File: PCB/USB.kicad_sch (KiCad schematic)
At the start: 30 parts, among them J1 DX07S024JJ2R1300, Q6 AGM612AP, U3 TPD4S480RUKR

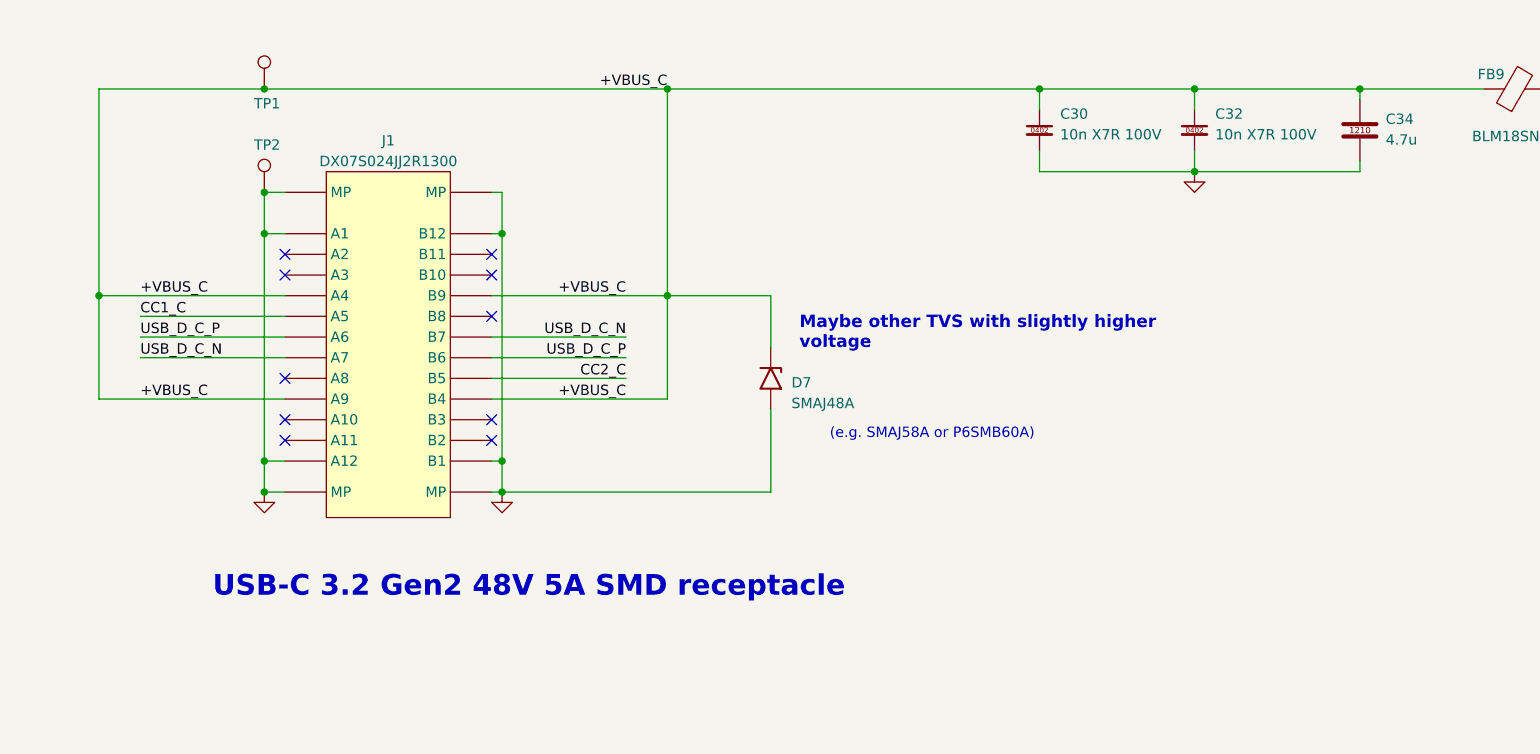
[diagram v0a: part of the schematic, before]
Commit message: Changed inductor to much better one
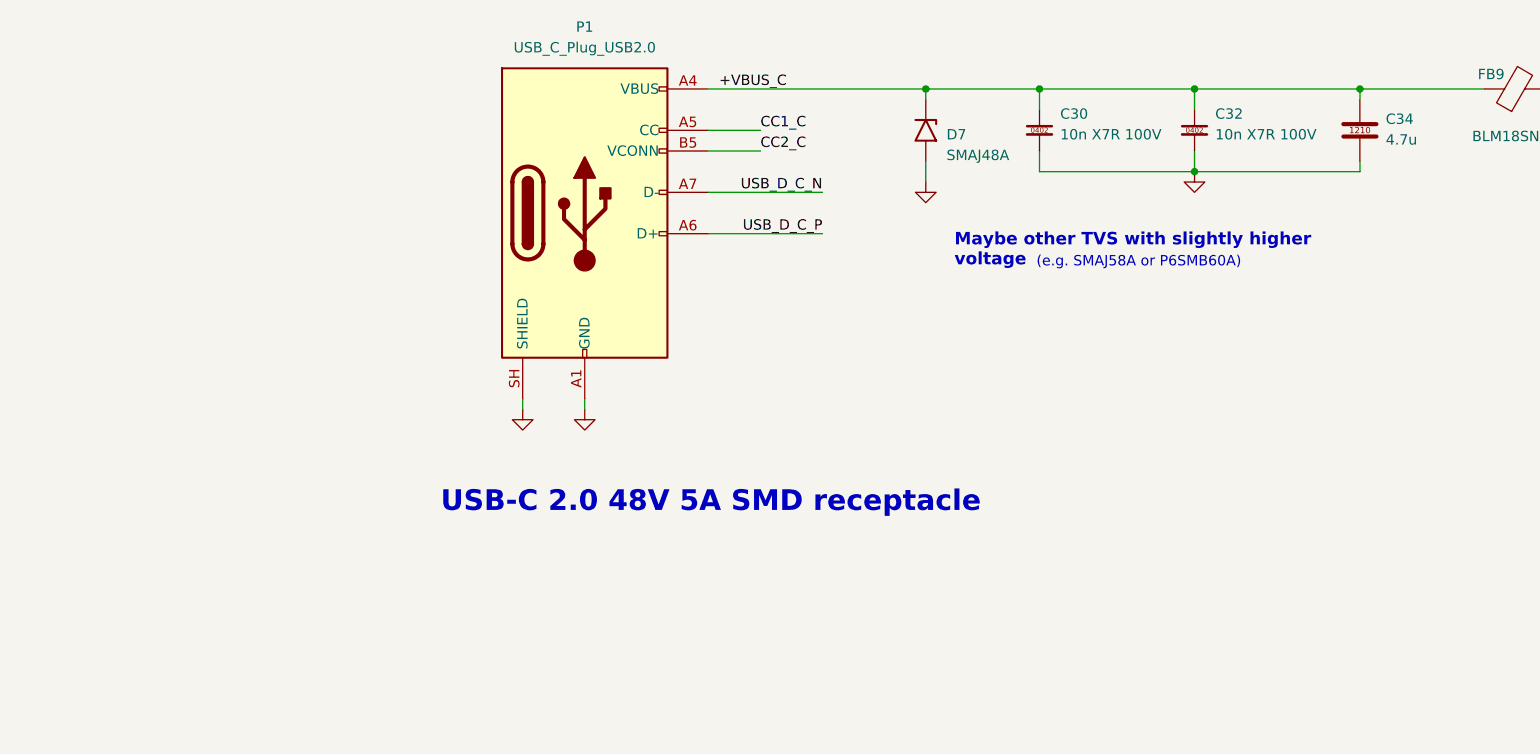
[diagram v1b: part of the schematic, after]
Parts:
- removed J1: DX07S024JJ2R1300, Altium_port:DX07S024JJ2R1300, symbol 0_PD240W:DX07S024JJ2R1300
- removed TP1, TP2: sp_oval_300x100, TestPoint:TestPoint_Pad_2.5x2.5mm, symbol Connector:TestPoint
- added P1: USB_C_Plug_USB2.0, Connector_USB:USB_C_Receptacle_GCT_USB4105-xx-A_16P_TopMnt_Horizontal, symbol Connector:USB_C_Plug_USB2.0
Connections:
- net +VBUS_C: now also P1.A4 (VBUS), P1.A9 (VBUS), P1.B4 (VBUS), P1.B9 (VBUS)
- net CC1_C: now also P1.A5 (CC)
- net CC2_C: now also P1.B5 (VCONN)
- net GND: now also P1.A1 (GND), P1.A12 (GND), P1.B1 (GND), P1.B12 (GND), P1.SH (SHIELD)
- net USB_D_C_N: now also P1.A7 (D-)
- net USB_D_C_P: now also P1.A6 (D+)
- no-connect marks 10 -> 0
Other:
- note added: "USB-C 2.0 48V 5A SMD receptacle"
- note removed: "USB-C 3.2 Gen2 48V 5A SMD receptacle"
- moved on the sheet: D7

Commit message: Preliminary finish of Rev3
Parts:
- removed D10: APTD1608LQBC/D, Altium_port:kingbright_0603_blue, symbol 0_PD240W:APTD1608LQBC/D
- removed R26, R27: 100k, Resistor_SMD:R_0402_1005Metric, symbol Device:R_Small
- removed R29: 33k 1%, Resistor_SMD:R_0402_1005Metric, symbol 0_passives:R_0402
- P1: footprint Connector_USB:USB_C_Receptacle_GCT_USB4105-xx-A_16P_TopMnt_Horizontal -> thommys-parts2:USB_C_Receptacle_GCT_USB4105-xx-A_16P_TopMnt_Horizontal
